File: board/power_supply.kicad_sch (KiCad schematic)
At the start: 31 parts, among them Q1 BSH203,215, Q2 BSH203,215, Q3 BSH203,215, SW1 MAIN, U5 LM1117-5.0, U6 NCV8165, U7 NCP115, U8 MIC5209

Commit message: finished layout for review
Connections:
- net +5V: now also U5.4 (VO)
- now unconnected: U6.2 (NC), U6.3 (NC), U6.6 (NC), U6.7 (NC)
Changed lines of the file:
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@@
       (effects (font (size 1.27 1.27)) hide)
     )
+    (pin "4")
     (pin "1")
     (pin "2")

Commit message: did some minor stuff
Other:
- company: (none) -> Hochschule Pforzheim
- title: (none) -> eduSignal
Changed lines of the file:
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@@
 (kicad_sch (version 20211123) (generator eeschema)
   (paper "A4")
+  (title_block
+    (title "eduSignal")
+    (date "2022-07-14")
+    (rev "1")
+    (company "Hochschule Pforzheim")
+    (comment 1 "Patrick Hanner")
+    (comment 2 "Biosignal development board")
+  )
   (junction (at 53.34 163.83) (diameter 0) (color 0 0 0 0)
   )

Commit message: worked feedback into layout with dp
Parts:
- added C51, C52: 100n, Capacitor_SMD:C_0402_1005Metric, symbol Device:C_Small
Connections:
- net +3.3VA: now also C51.2
- net +5VA: now also C52.2
- net GND: now also C51.1, C52.1
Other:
- note removed: "Disable Power?"
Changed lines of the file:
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@@
   (junction (at 121.92 44.45) (diameter 0) (color 0 0 0 0)
   )
+  (junction (at 198.12 21.59) (diameter 0) (color 0 0 0 0)
+  )
   (junction (at 223.52 67.31) (diameter 0) (color 0 0 0 0)
   )
@@
   (junction (at 260.35 67.31) (diameter 0) (color 0 0 0 0)
   )
+  (junction (at 198.12 26.67) (diameter 0) (color 0 0 0 0)
+  )
   (junction (at 176.53 44.45) (diameter 0) (color 0 0 0 0)
   )
@@
   )
   (junction (at 269.24 54.61) (diameter 0) (color 0 0 0 0)
-  )
-  (junction (at 198.12 29.21) (diameter 0) (color 0 0 0 0)
   )
   (junction (at 229.87 54.61) (diameter 0) (color 0 0 0 0)
@@
     (stroke (width 0) (type default) (color 0 0 0 0))
   )
+  (wire (pts (xy 262.89 48.26) (xy 269.24 48.26))
+    (stroke (width 0) (type default) (color 0 0 0 0))
+  )
   (wire (pts (xy 104.14 41.91) (xy 104.14 44.45))
     (stroke (width 0) (type default) (color 0 0 0 0))
@@
     (stroke (width 0) (type solid) (color 0 0 0 0))
   )
+  (wire (pts (xy 198.12 26.67) (xy 212.09 26.67))
+    (stroke (width 0) (type default) (color 0 0 0 0))
+  )
   (wire (pts (xy 260.35 54.61) (xy 260.35 55.88))
     (stroke (width 0) (type default) (color 0 0 0 0))
@@
     (stroke (width 0) (type solid) (color 0 0 0 0))
   )
-  (wire (pts (xy 198.12 29.21) (xy 198.12 30.48))
+  (wire (pts (xy 198.12 26.67) (xy 198.12 30.48))
     (stroke (width 0) (type default) (color 0 0 0 0))
   )
@@
     (stroke (width 0) (type default) (color 0 0 0 0))
   )
+  (wire (pts (xy 198.12 21.59) (xy 198.12 26.67))
+    (stroke (width 0) (type default) (color 0 0 0 0))
+  )
   (wire (pts (xy 231.14 62.23) (xy 229.87 62.23))
     (stroke (width 0) (type default) (color 0 0 0 0))
   )
+  (wire (pts (xy 262.89 41.91) (xy 262.89 48.26))
+    (stroke (width 0) (type default) (color 0 0 0 0))
+  )
   (wire (pts (xy 53.34 36.83) (xy 50.165 36.83))
     (stroke (width 0) (type default) (color 0 0 0 0))
@@
     (stroke (width 0) (type default) (color 0 0 0 0))
   )
-  (wire (pts (xy 198.12 29.21) (xy 200.66 29.21))
+  (wire (pts (xy 198.12 21.59) (xy 200.66 21.59))
     (stroke (width 0) (type default) (color 0 0 0 0))
   )
@@
     (stroke (width 0) (type default) (color 0 0 0 0))
   )
-  (wire (pts (xy 198.12 27.94) (xy 198.12 29.21))
+  (wire (pts (xy 198.12 20.32) (xy 198.12 21.59))
     (stroke (width 0) (type default) (color 0 0 0 0))
   )
@@
     (stroke (width 0) (type default) (color 0 0 0 0))
   )
+  (wire (pts (xy 260.35 41.91) (xy 262.89 41.91))
+    (stroke (width 0) (type default) (color 0 0 0 0))
+  )
   (wire (pts (xy 176.53 44.45) (xy 186.69 44.45))
     (stroke (width 0) (type default) (color 0 0 0 0))
@@
   (wire (pts (xy 214.63 52.07) (xy 214.63 54.61))
     (stroke (width 0) (type default) (color 0 0 0 0))
-  )
-  (text "Disable Power?" (at 207.01 74.93 0)
-    (effects (font (size 1.27 1.27)) (justify left bottom))
   )
   (text "I2C devices power switching" (at 13.97 152.4 0)
@@
     (effects (font (size 1.27 1.27)) (justify right))
   )
-  (symbol (lib_id "power:+3.3VA") (at 198.12 27.94 0) (unit 1)
-    (in_bom yes) (on_board yes) (fields_autoplaced)
-    (property "Reference" "#PWR052" (id 0) (at 198.12 31.75 0)
-      (effects (font (size 1.27 1.27)) hide)
-    )
-    (property "Value" "+3.3VA" (id 1) (at 198.12 22.86 0))
-    (property "Footprint" "" (id 2) (at 198.12 27.94 0)
-      (effects (font (size 1.27 1.27)) hide)
-    )
-    (property "Datasheet" "" (id 3) (at 198.12 27.94 0)
+  (symbol (lib_id "power:+3.3VA") (at 198.12 20.32 0) (unit 1)
+    (in_bom yes) (on_board yes) (fields_autoplaced)
+    (property "Reference" "#PWR052" (id 0) (at 198.12 24.13 0)
+      (effects (font (size 1.27 1.27)) hide)
+    )
+    (property "Value" "+3.3VA" (id 1) (at 198.12 15.24 0))
+    (property "Footprint" "" (id 2) (at 198.12 20.32 0)
+      (effects (font (size 1.27 1.27)) hide)
+    )
+    (property "Datasheet" "" (id 3) (at 198.12 20.32 0)
       (effects (font (size 1.27 1.27)) hide)
     )
@@
     (pin "2")
   )
+  (symbol (lib_id "Device:C_Small") (at 257.81 41.91 90) (unit 1)
+    (in_bom yes) (on_board yes) (fields_autoplaced)
+    (property "Reference" "C52" (id 0) (at 259.0865 44.45 0)
+      (effects (font (size 1.27 1.27)) (justify right))
+    )
+    (property "Value" "100n" (id 1) (at 256.5465 44.45 0)
+      (effects (font (size 1.27 1.27)) (justify right))
+    )
+    (property "Footprint" "Capacitor_SMD:C_0402_1005Metric" (id 2) (at 257.81 41.91 0)
+      (effects (font (size 1.27 1.27)) hide)
+    )
+    (property "Datasheet" "~" (id 3) (at 257.81 41.91 0)
+      (effects (font (size 1.27 1.27)) hide)
+    )
+    (pin "1")
+    (pin "2")
+  )
   (symbol (lib_id "Device:C_Small") (at 269.24 58.42 0) (unit 1)
     (in_bom yes) (on_board yes) (fields_autoplaced)
@@
     (pin "1")
     (pin "2")
+  )
+  (symbol (lib_id "power:GND") (at 255.27 41.91 270) (mirror x) (unit 1)
+    (in_bom yes) (on_board yes)
+    (property "Reference" "#PWR0106" (id 0) (at 248.92 41.91 0)
+      (effects (font (size 1.27 1.27)) hide)
+    )
+    (property "Value" "GND" (id 1) (at 250.825 43.8151 0)
+      (effects (font (size 1.27 1.27)) (justify left))
+    )
+    (property "Footprint" "" (id 2) (at 255.27 41.91 0)
+      (effects (font (size 1.27 1.27)) hide)
+    )
+    (property "Datasheet" "" (id 3) (at 255.27 41.91 0)
+      (effects (font (size 1.27 1.27)) hide)
+    )
+    (pin "1")
+  )
+  (symbol (lib_id "power:GND") (at 212.09 31.75 0) (mirror y) (unit 1)
+    (in_bom yes) (on_board yes)
+    (property "Reference" "#PWR0105" (id 0) (at 212.09 38.1 0)
+      (effects (font (size 1.27 1.27)) hide)
+    )
+    (property "Value" "GND" (id 1) (at 213.9951 36.195 0)
+      (effects (font (size 1.27 1.27)) (justify left))
+    )
+    (property "Footprint" "" (id 2) (at 212.09 31.75 0)
+      (effects (font (size 1.27 1.27)) hide)
+    )
+    (property "Datasheet" "" (id 3) (at 212.09 31.75 0)
+      (effects (font (size 1.27 1.27)) hide)
+    )
+    (pin "1")
   )
   (symbol (lib_id "Device:Q_PMOS_GSD") (at 53.34 25.4 90) (unit 1)
@@
     (pin "1")
   )
-  (symbol (lib_id "power:PWR_FLAG") (at 200.66 29.21 270) (unit 1)
-    (in_bom yes) (on_board yes) (fields_autoplaced)
-    (property "Reference" "#FLG0104" (id 0) (at 202.565 29.21 0)
-      (effects (font (size 1.27 1.27)) hide)
-    )
-    (property "Value" "PWR_FLAG" (id 1) (at 204.47 29.2099 90)
-      (effects (font (size 1.27 1.27)) (justify left))
-    )
-    (property "Footprint" "" (id 2) (at 200.66 29.21 0)
-      (effects (font (size 1.27 1.27)) hide)
-    )
-    (property "Datasheet" "~" (id 3) (at 200.66 29.21 0)
+  (symbol (lib_id "power:PWR_FLAG") (at 200.66 21.59 270) (unit 1)
+    (in_bom yes) (on_board yes) (fields_autoplaced)
+    (property "Reference" "#FLG0104" (id 0) (at 202.565 21.59 0)
+      (effects (font (size 1.27 1.27)) hide)
+    )
+    (property "Value" "PWR_FLAG" (id 1) (at 204.47 21.5899 90)
+      (effects (font (size 1.27 1.27)) (justify left))
+    )
+    (property "Footprint" "" (id 2) (at 200.66 21.59 0)
+      (effects (font (size 1.27 1.27)) hide)
+    )
+    (property "Datasheet" "~" (id 3) (at 200.66 21.59 0)
       (effects (font (size 1.27 1.27)) hide)
     )
@@
   )
   (symbol (lib_id "Device:FerriteBead_Small") (at 198.12 33.02 0) (unit 1)
-    (in_bom yes) (on_board yes) (fields_autoplaced)
+    (in_bom yes) (on_board yes)
     (property "Reference" "FB1" (id 0) (at 200.66 31.7118 0)
       (effects (font (size 1.27 1.27)) (justify left))
@@
       (effects (font (size 1.27 1.27)) hide)
     )
+    (pin "1")
+    (pin "2")
+  )
+  (symbol (lib_id "Device:C_Small") (at 212.09 29.21 180) (unit 1)
+    (in_bom yes) (on_board yes) (fields_autoplaced)
+    (property "Reference" "C51" (id 0) (at 214.63 27.9335 0)
+      (effects (font (size 1.27 1.27)) (justify right))
+    )
+    (property "Value" "100n" (id 1) (at 214.63 30.4735 0)
+      (effects (font (size 1.27 1.27)) (justify right))
+    )
+    (property "Footprint" "Capacitor_SMD:C_0402_1005Metric" (id 2) (at 212.09 29.21 0)
+      (effects (font (size 1.27 1.27)) hide)
+    )
+    (property "Datasheet" "~" (id 3) (at 212.09 29.21 0)
+      (effects (font (size 1.27 1.27)) hide)
+    )

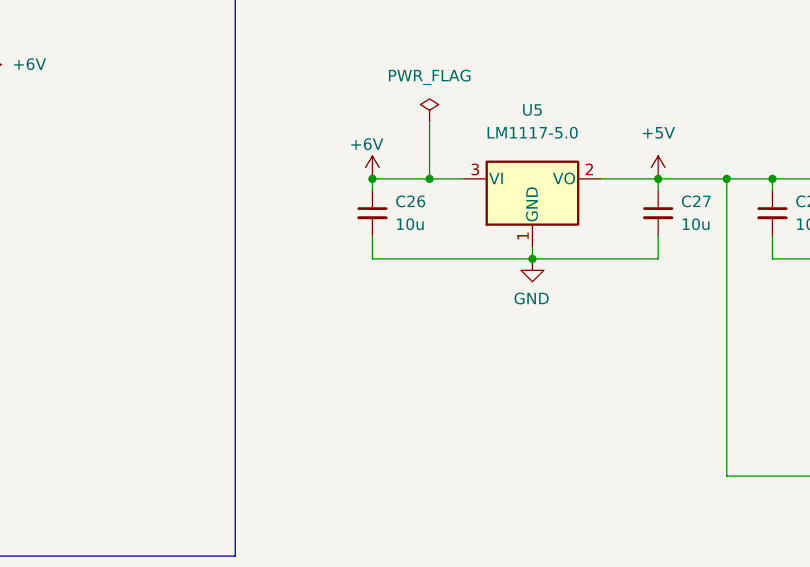
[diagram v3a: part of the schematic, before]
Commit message: fixed errors in schematic
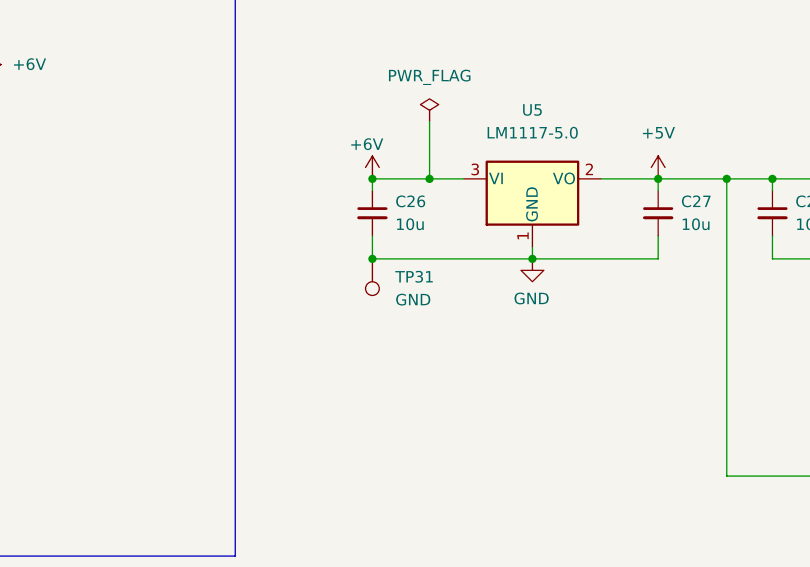
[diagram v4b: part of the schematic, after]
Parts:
- added TP31: GND, TestPoint:TestPoint_Keystone_5015_Micro-Minature, symbol Connector:TestPoint
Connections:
- net GND: now also TP31.1
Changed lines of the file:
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@@
   (junction (at 165.1 68.58) (diameter 0) (color 0 0 0 0)
+  )
+  (junction (at 104.14 44.45) (diameter 0) (color 0 0 0 0)
   )
   (junction (at 53.34 36.83) (diameter 0) (color 0 0 0 0)
@@
     (pin "2")
   )
+  (symbol (lib_id "Connector:TestPoint") (at 104.14 44.45 180) (unit 1)
+    (in_bom yes) (on_board yes) (fields_autoplaced)
+    (property "Reference" "TP31" (id 0) (at 106.68 46.4819 0)
+      (effects (font (size 1.27 1.27)) (justify right))
+    )
+    (property "Value" "GND" (id 1) (at 106.68 49.0219 0)
+      (effects (font (size 1.27 1.27)) (justify right))
+    )
+    (property "Footprint" "TestPoint:TestPoint_Keystone_5015_Micro-Minature" (id 2) (at 99.06 44.45 0)
+      (effects (font (size 1.27 1.27)) hide)
+    )
+    (property "Datasheet" "~" (id 3) (at 99.06 44.45 0)
+      (effects (font (size 1.27 1.27)) hide)
+    )
+    (pin "1")
+  )
   (symbol (lib_id "Device:C_Small") (at 198.12 39.37 0) (unit 1)
